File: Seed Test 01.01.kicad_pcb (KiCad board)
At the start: 2 copper layers, 124 parts, among them J1 Daisy_Seed_Temp, J10 1VOCT1_IN, J11 1VOCT2_IN, J12 MAIN_OUT1, J13 MAIN_OUT2, J14 MAIN_OUT4, J15 MAIN_OUT3, J2 DISP_3_128X64, J3 Micro_SD_Card, J4 EURO_PWR, J5 CV1_INPUT, J6 CV2_INPUT, J7 CV3_INPUT, J8 CV4_INPUT, J9 GATE_TRIGGER_IN, Q1 MMBT3904, SW1 RotaryEncoder_Switch, U1 CS4334, U2 AP2204K-3.3, U3 LM1117-5.0, U4 LM4040DBZ-5, U5 MCP6004, U6 TL074, U7 TL074, U8 MCP6002-xMC

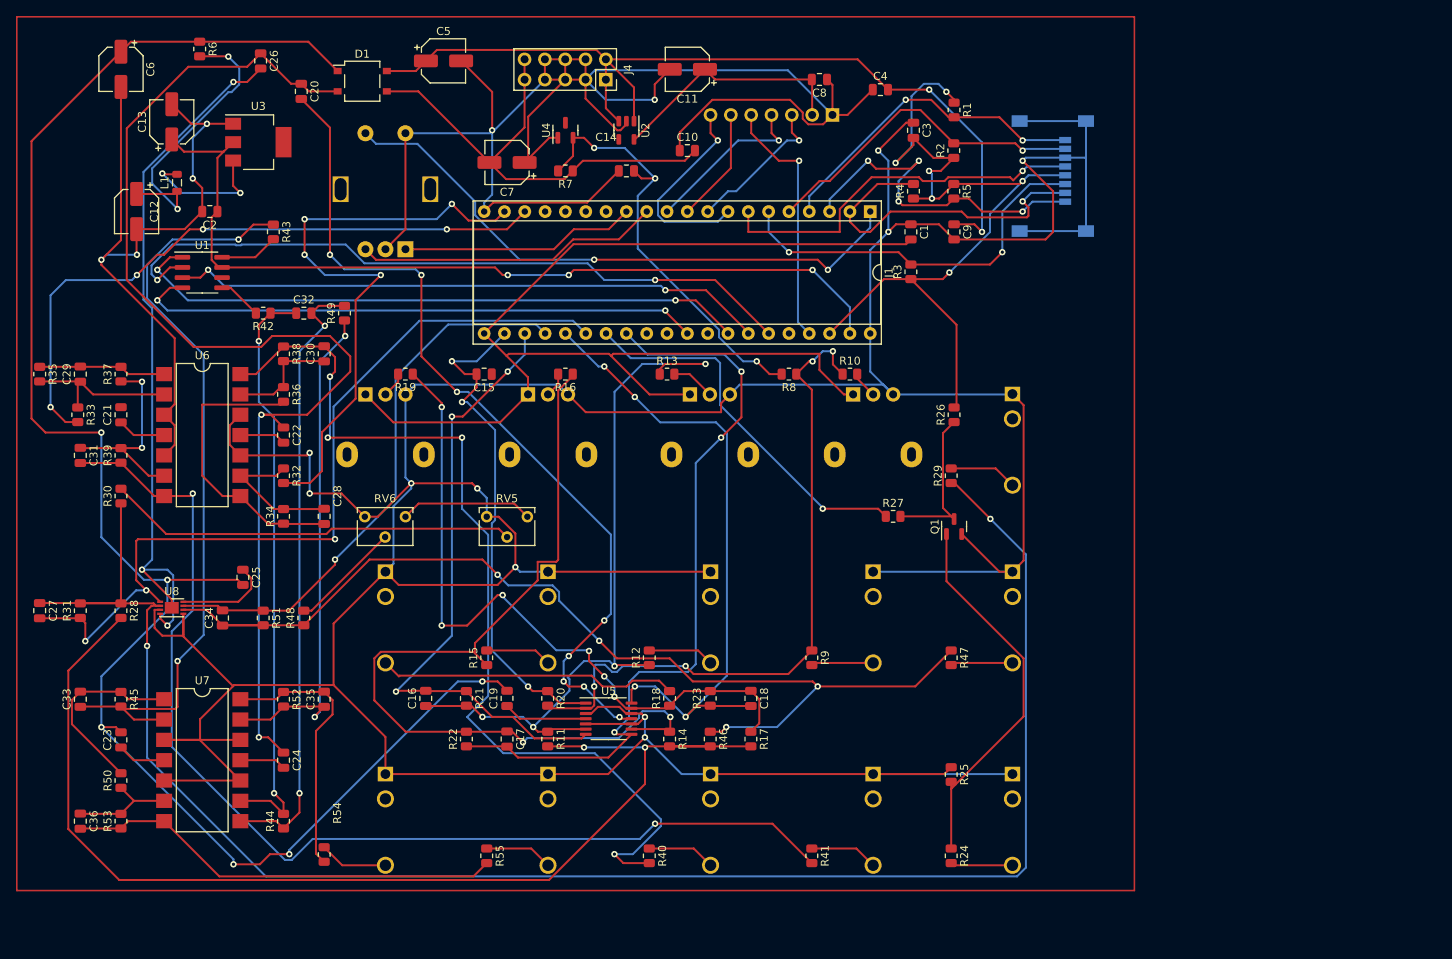
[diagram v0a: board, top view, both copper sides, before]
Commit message: updated power rails error
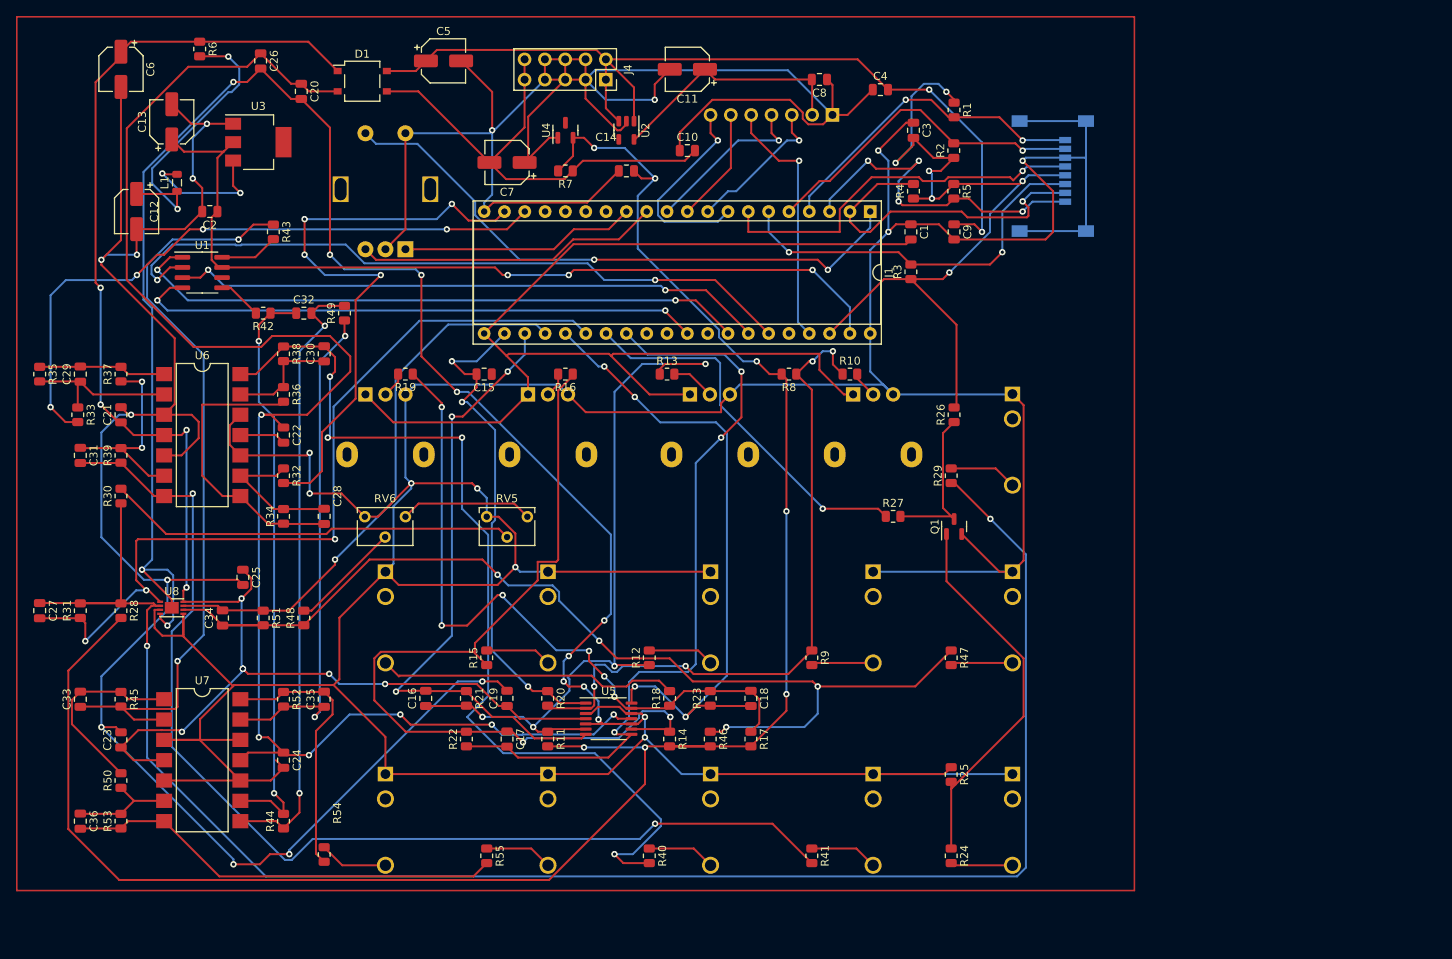
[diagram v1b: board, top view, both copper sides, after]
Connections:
- C19 pad 1: Net-(C19-Pad1) -> +12V
- C19 pad 2: +12V -> GNDA
- C20 pad 2: Net-(C20-Pad2) -> GNDA
- C21 pad 1: Net-(C21-Pad1) -> +12V
- C21 pad 2: +12V -> GNDA
- C22 pad 2: Net-(C22-Pad2) -> GNDA
- C23 pad 1: Net-(C23-Pad1) -> +12V
- C23 pad 2: +12V -> GNDA
- C24 pad 2: Net-(C24-Pad2) -> GNDA
- C25 pad 1: Net-(C25-Pad1) -> +12V
- C25 pad 2: +12V -> GNDA
- C26 pad 2: Net-(C26-Pad2) -> GNDA
- U5 pad 11: Net-(C20-Pad2) -> -12V
- U5 pad 4: Net-(C19-Pad1) -> +12V
- U6 pad 11: Net-(C22-Pad2) -> -12V
- U6 pad 4: Net-(C21-Pad1) -> +12V
- U7 pad 11: Net-(C24-Pad2) -> -12V
- U7 pad 4: Net-(C23-Pad1) -> +12V
- U8 pad 4: Net-(C26-Pad2) -> -12V
- U8 pad 8: Net-(C25-Pad1) -> +12V
- U8 pad 9: Net-(C26-Pad2) -> -12V
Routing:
- net GNDA: track 873.0 -> 1136.3 mm, vias 16 -> 30
- net -12V: track 206.5 -> 355.7 mm, vias 2 -> 9
- net Net-(C20-Pad2): track 107.7 -> 0.00 mm, vias 8 -> 0
- net Net-(C26-Pad2): track 89.6 -> 0.00 mm, vias 3 -> 0
- net -10V: track 199.0 -> 247.6 mm, vias 5 -> 7
- net +12V: track 328.2 -> 313.6 mm, vias 8 -> 12
- net Net-(C25-Pad1): track 12.0 -> 0.00 mm
- net Net-(C19-Pad1): track 10.5 -> 0.00 mm
- net Net-(C23-Pad1): track 6.05 -> 0.00 mm
- net Net-(C21-Pad1): track 6.05 -> 0.00 mm
- net Net-(C24-Pad2): track 5.79 -> 0.00 mm
- net Net-(C22-Pad2): track 5.79 -> 0.00 mm
- net Net-(C34-Pad1): track 130.1 -> 132.1 mm

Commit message: Version update
Added DC/DC power block and opAmps for audio input. Redesigned PCB completely moving all components to one side so that it can lay flat.
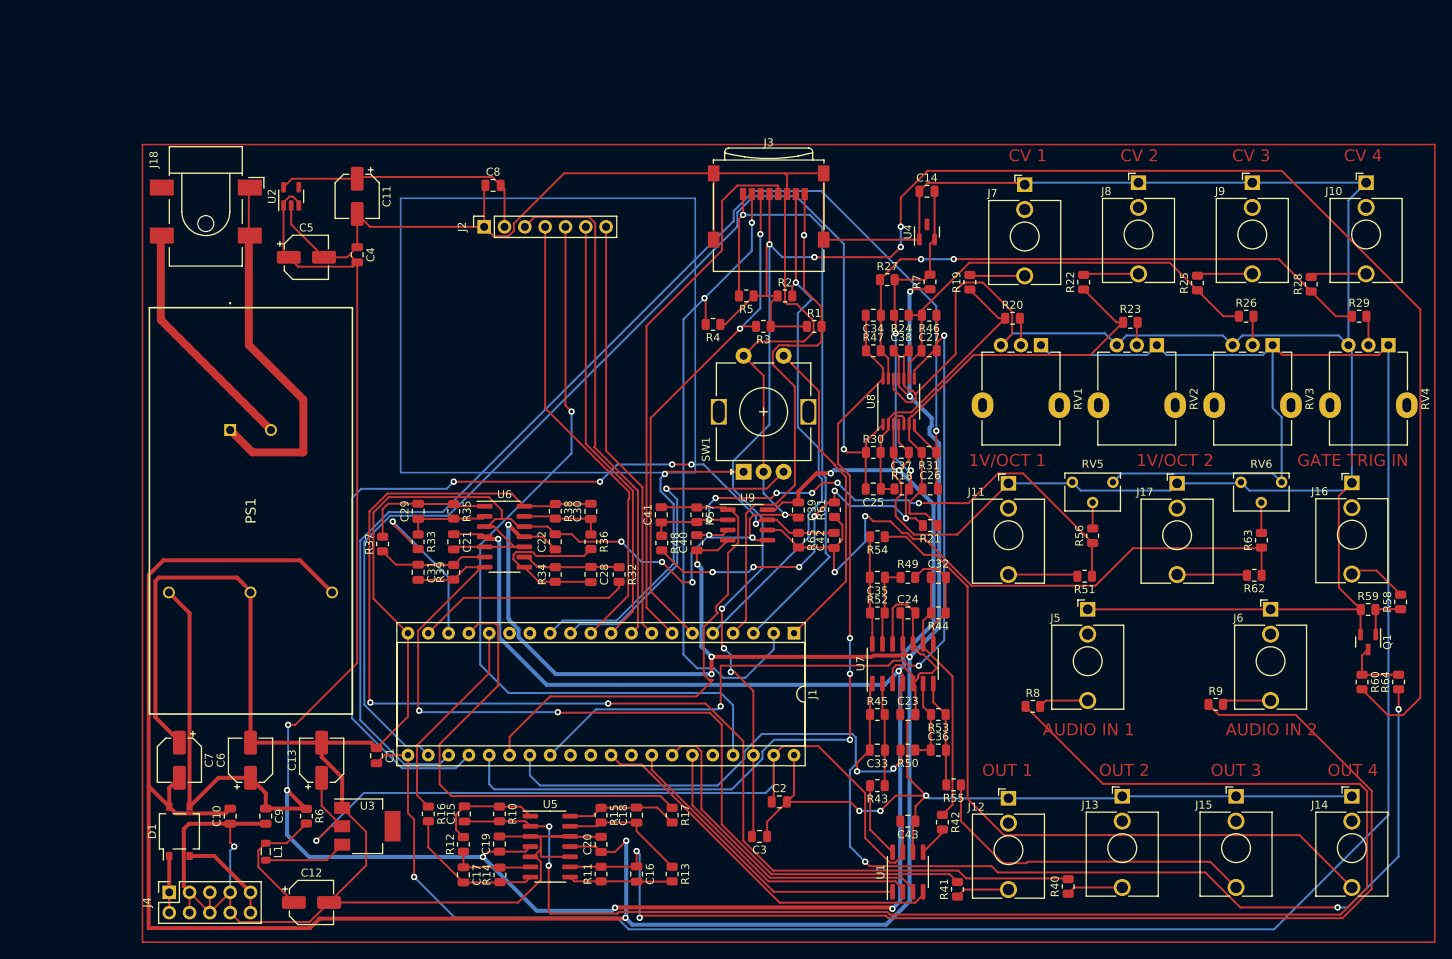
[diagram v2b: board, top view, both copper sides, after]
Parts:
- added C37: 100nF, Capacitor_SMD:C_0805_2012Metric, F.Cu at (163.9, 83.4)
- added C38: 100nF, Capacitor_SMD:C_0805_2012Metric, F.Cu at (163.9, 70.7)
- added C39: 100nF, Capacitor_SMD:C_0805_2012Metric, F.Cu at (151.0, 90.6)
- added C40: 100nF, Capacitor_SMD:C_0805_2012Metric, F.Cu at (138.3, 94.7)
- added C41: 10nF, Capacitor_SMD:C_0805_2012Metric, F.Cu at (133.9, 91.2)
- added C42: 10nF, Capacitor_SMD:C_0805_2012Metric, F.Cu at (155.5, 94.5)
- added C43: 100nF, Capacitor_SMD:C_0805_2012Metric, F.Cu at (164.7, 129.5)
- added J16: GATE_TRIGGER_IN, Connector_Audio:Jack_3.5mm_QingPu_WQP-PJ398SM_Vertical_CircularHoles, F.Cu at (220.2, 87.3)
- added J17: 1VOCT2_IN, Connector_Audio:Jack_3.5mm_QingPu_WQP-PJ398SM_Vertical_CircularHoles, F.Cu at (198.4, 87.3)
- added J18: Barrel_Jack_MountingPin, Connector_BarrelJack:BarrelJack_CLIFF_FC681465S_SMT_Horizontal, F.Cu at (77.0, 53.3)
- added PS1: DLW05A-12, KiCad:DLW05A12, F.Cu at (80.0, 80.7)
- added R56: 66.5k, Resistor_SMD:R_0805_2012Metric, F.Cu at (187.8, 93.9)
- added R57: 66.5k, Resistor_SMD:R_0805_2012Metric, F.Cu at (138.3, 91.2)
- added R58: 100k, Resistor_SMD:R_0805_2012Metric, F.Cu at (226.3, 102.1)
- added R59: 1M, Resistor_SMD:R_0805_2012Metric, F.Cu at (222.3, 103.1)
- added R60: 10k, Resistor_SMD:R_0805_2012Metric, F.Cu at (221.5, 112.1)
- added R61: 200k, Resistor_SMD:R_0805_2012Metric, F.Cu at (155.6, 90.6)
- added R62: 100k, Resistor_SMD:R_0805_2012Metric, F.Cu at (208.0, 98.8)
- added R63: 66.5k, Resistor_SMD:R_0805_2012Metric, F.Cu at (208.9, 94.4)
- added R64: 1k, Resistor_SMD:R_0805_2012Metric, F.Cu at (226.1, 112.1)
- added R65: 66.5k, Resistor_SMD:R_0805_2012Metric, F.Cu at (151.0, 94.4)
- added U9: MCP6002-xSN, Package_SO:SOIC-8_3.9x4.9mm_P1.27mm, F.Cu at (144.7, 92.5)
- C15, C16, C17, C18: value 10nF -> 47pF
- C25, C26: value 100nF -> 10nF
- J10: value 1VOCT1_IN -> CV4_INPUT; moved to F.Cu
- J11: value 1VOCT2_IN -> 1VOCT1_IN; moved to F.Cu
- J12, J13, J14, J15, J2, J3, RV1, RV2, RV3, RV4, SW1: moved to F.Cu
- J5: value CV1_INPUT -> AUDIO_IN_1L; moved to F.Cu
- J6: value CV2_INPUT -> AUDIO_IN_2R; moved to F.Cu
- J7: value CV3_INPUT -> CV1_INPUT; moved to F.Cu
- J8: value CV4_INPUT -> CV2_INPUT; moved to F.Cu
- J9: value GATE_TRIGGER_IN -> CV3_INPUT; moved to F.Cu
- R10, R13, R19, R22, R51: value 66.5k -> 100k
- R11, R14, R28, R8: value 200k -> 100k
- R16: value 66.5k -> 1k
- R17: value 200k -> 1k
- R18, R24: value 100k -> 200k
- R21, R48: value 66.5k -> 200k
- R25: value 1M -> 100k
- R26: value 10k -> 66.5k
- R27: value 1k -> 200k
- R29, R47: value 100k -> 66.5k
- R46: value 200k -> 66.5k
- U5: value MCP6004 -> TL074; footprint Package_SO:TSSOP-14_4.4x5mm_P0.65mm -> Package_SO:SOIC-14_3.9x8.7mm_P1.27mm
- U6, U7: footprint Package_DIP:SMDIP-14_W9.53mm -> Package_SO:SOIC-14_3.9x8.7mm_P1.27mm
- U8: value MCP6002-xMC -> MCP6004; footprint Package_DFN_QFN:DFN-8-1EP_3x2mm_P0.5mm_EP1.75x1.45mm -> Package_SO:TSSOP-14_4.4x5mm_P0.65mm
- moved R28 154.3 mm to (215.1, 62.4), turned to 90 degrees
- moved RV4 128.0 mm to (224.8, 70.0)
- moved J14 120.8 mm to (220.2, 126.4), turned to 0 degrees
- moved C27 115.8 mm to (167.4, 70.7), turned to 0 degrees
- moved U1 115.7 mm to (164.7, 135.9), turned to 90 degrees
- moved J4 115.3 mm to (72.4, 138.4), turned to 90 degrees
- moved C9 112.9 mm to (84.5, 128.9)
- moved RV6 109.6 mm to (211.4, 87.2)
- moved R31 107.9 mm to (167.4, 83.4), turned to 180 degrees
- moved C36 107.6 mm to (168.5, 120.7), turned to 0 degrees
- moved R42 106.1 mm to (169.0, 129.7), turned to -90 degrees
- moved J8 106.0 mm to (193.6, 49.7), turned to 0 degrees
- moved R53 103.0 mm to (168.5, 116.2), turned to 180 degrees
- moved R51 102.8 mm to (186.8, 98.9), turned to 180 degrees
- moved C2 102.5 mm to (148.7, 127.1), turned to 0 degrees
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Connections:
- C15 pad 2: ADC_CTRL_1 -> Net-(C15-Pad2)
- C16 pad 2: ADC_CTRL_2 -> Net-(C16-Pad2)
- C17 pad 2: ADC_CTRL_3 -> Net-(C17-Pad2)
- C18 pad 2: ADC_CTRL_4 -> Net-(C18-Pad2)
- C25 pad 1: +12V -> Net-(C25-Pad1)
- C25 pad 2: GNDA -> ADC_CTRL_1
- C26 pad 1: -12V -> Net-(C26-Pad1)
- C26 pad 2: GNDA -> ADC_CTRL_2
- C27 pad 2: ADC1_1VOCT1 -> ADC_CTRL_3
- C34 pad 2: ADC1_1VOCT2 -> ADC_CTRL_4
- D1 pad 1: +12V -> VCC
- D1 pad 2: -12V -> VEE
- D1 pad 3: -12V -> +12V
- D1 pad 4: +12V -> -12V
- J4 pad 1: +12V -> VCC
- J4 pad 10: -12V -> VEE
- J4 pad 2: +12V -> VCC
- J4 pad 9: -12V -> VEE
- R10 pad 1: Net-(C15-Pad1) -> Net-(C15-Pad2)
- R10 pad 2: Net-(R10-Pad2) -> Net-(C15-Pad1)
- R11 pad 1: Net-(C16-Pad1) -> Net-(C16-Pad2)
- R11 pad 2: -10V -> Net-(C16-Pad1)
- R12 pad 1: Net-(C16-Pad1) -> Net-(C17-Pad1)
- R12 pad 2: Net-(J6-PadT) -> Net-(C15-Pad2)
- R13 pad 1: Net-(C16-Pad1) -> Net-(C18-Pad1)
- R13 pad 2: Net-(R13-Pad2) -> Net-(C16-Pad2)
- R14 pad 1: Net-(C17-Pad1) -> Net-(C17-Pad2)
- R14 pad 2: -10V -> Net-(C17-Pad1)
- R15 pad 1: Net-(C17-Pad1) -> Net-(C18-Pad2)
- R15 pad 2: Net-(J7-PadT) -> Net-(C18-Pad1)
- R16 pad 1: Net-(C17-Pad1) -> AUDIO_IN_L
- R16 pad 2: Net-(R16-Pad2) -> Net-(C17-Pad2)
- R17 pad 1: Net-(C18-Pad1) -> AUDIO_IN_R
- R17 pad 2: -10V -> Net-(C18-Pad2)
- R18 pad 1: Net-(C18-Pad1) -> Net-(C25-Pad1)
- R18 pad 2: Net-(J8-PadT) -> -10V
- R19 pad 1: Net-(C18-Pad1) -> Net-(C25-Pad1)
- R19 pad 2: Net-(R19-Pad2) -> Net-(J7-PadT)
- R20 pad 1: ADC_CTRL_1 -> Net-(C25-Pad1)
- R20 pad 2: Net-(C15-Pad1) -> Net-(R20-Pad2)
- R21 pad 1: ADC_CTRL_2 -> Net-(C26-Pad1)
- R21 pad 2: Net-(C16-Pad1) -> -10V
- R22 pad 1: ADC_CTRL_3 -> Net-(C26-Pad1)
- R22 pad 2: Net-(C17-Pad1) -> Net-(J8-PadT)
- R23 pad 1: ADC_CTRL_4 -> Net-(C26-Pad1)
- R23 pad 2: Net-(C18-Pad1) -> Net-(R23-Pad2)
- R24 pad 1: Net-(Q1-Pad1) -> Net-(C27-Pad1)
- R24 pad 2: Net-(J9-PadT) -> -10V
- R25 pad 1: GNDA -> Net-(C27-Pad1)
- R25 pad 2: Net-(Q1-Pad1) -> Net-(J9-PadT)
- R26 pad 1: Net-(Q1-Pad3) -> Net-(C27-Pad1)
- R26 pad 2: +3.3VA -> Net-(R26-Pad2)
- R27 pad 1: ADC1_GATE_IN -> Net-(C34-Pad1)
- R27 pad 2: Net-(Q1-Pad3) -> -10V
- R28 pad 1: Net-(C27-Pad1) -> Net-(C34-Pad1)
- R28 pad 2: -10V -> Net-(J10-PadT)
- R29 pad 1: Net-(C27-Pad1) -> Net-(C34-Pad1)
- R29 pad 2: Net-(J10-PadT) -> Net-(R29-Pad2)
- R30 pad 1: Net-(C27-Pad1) -> ADC_CTRL_1
- R30 pad 2: Net-(R30-Pad2) -> Net-(C25-Pad1)
- R31 pad 1: ADC1_1VOCT1 -> ADC_CTRL_2
- R31 pad 2: Net-(C27-Pad1) -> Net-(C26-Pad1)
- R46 pad 1: Net-(C34-Pad1) -> ADC_CTRL_3
- R46 pad 2: -10V -> Net-(C27-Pad1)
- R47 pad 1: Net-(C34-Pad1) -> ADC_CTRL_4
- R47 pad 2: Net-(J11-PadT) -> Net-(C34-Pad1)
- R48 pad 1: Net-(C34-Pad1) -> Net-(C41-Pad1)
- R48 pad 2: Net-(R48-Pad2) -> -10V
- R51 pad 1: ADC1_1VOCT2 -> Net-(C41-Pad1)
- R51 pad 2: Net-(C34-Pad1) -> Net-(J11-PadT)
- R8 pad 2: -10V -> Net-(J5-PadT)
- R9 pad 1: Net-(C15-Pad1) -> Net-(C16-Pad1)
- R9 pad 2: Net-(J5-PadT) -> Net-(J6-PadT)
- RV1 pad 2: Net-(R10-Pad2) -> Net-(R20-Pad2)
- RV2 pad 2: Net-(R13-Pad2) -> Net-(R23-Pad2)
- RV3 pad 2: Net-(R16-Pad2) -> Net-(R26-Pad2)
- RV4 pad 2: Net-(R19-Pad2) -> Net-(R29-Pad2)
- RV5 pad 2: Net-(R30-Pad2) -> Net-(R56-Pad2)
- RV6 pad 2: Net-(R48-Pad2) -> Net-(R63-Pad2)
- U5 pad 1: ADC_CTRL_1 -> Net-(C15-Pad2)
- U5 pad 14: ADC_CTRL_4 -> Net-(C18-Pad2)
- U5 pad 6: Net-(C16-Pad1) -> Net-(C17-Pad1)
- U5 pad 7: ADC_CTRL_2 -> Net-(C17-Pad2)
- U5 pad 8: ADC_CTRL_3 -> Net-(C16-Pad2)
- U5 pad 9: Net-(C17-Pad1) -> Net-(C16-Pad1)
- U8 pad 1: ADC1_1VOCT1 -> ADC_CTRL_1
- U8 pad 2: Net-(C27-Pad1) -> Net-(C25-Pad1)
- U8 pad 4: -12V -> +12V
- U8 pad 6: Net-(C34-Pad1) -> Net-(C26-Pad1)
- U8 pad 7: ADC1_1VOCT2 -> ADC_CTRL_2
- U8 pad 8: +12V -> ADC_CTRL_3
- U8 pad 9: -12V -> Net-(C27-Pad1)
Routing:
- net GNDA: track 1136.3 -> 950.0 mm, vias 30 -> 10
- net Net-(C27-Pad1): track 221.2 -> 55.7 mm, vias 2 -> 0
- net +3.3VA: track 106.0 -> 267.1 mm, vias 6 -> 7
- net -10V: track 247.6 -> 89.8 mm, vias 7 -> 8
- net +3.3VP: track 166.7 -> 295.1 mm, vias 0 -> 1
- net ADC1_GATE_IN: track 47.6 -> 156.4 mm, vias 1 -> 3
- net Net-(C15-Pad1): track 85.1 -> 184.8 mm, vias 4 -> 2
- net Net-(C17-Pad1): track 109.8 -> 10.4 mm, vias 2 -> 0
- net ADC_CTRL_1: track 63.7 -> 149.9 mm, vias 3 -> 1
- net Net-(C42-Pad1): track 0.00 -> 84.2 mm, vias 0 -> 2
- net Net-(J14-PadT): track 8.60 -> 92.1 mm
- net Net-(C33-Pad1): track 95.9 -> 12.9 mm, vias 2 -> 0
- net ADC_CTRL_2: track 78.7 -> 160.6 mm, vias 3 -> 1
- net +12V: track 313.6 -> 394.6 mm, vias 12 -> 9
- net Net-(C18-Pad1): track 87.5 -> 15.9 mm, vias 6 -> 0
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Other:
- board text added: "1V/OCT 1"
- board text added: "1V/OCT 2"
- board text added: "AUDIO IN 1"
- board text added: "AUDIO IN 2"
- board text added: "CV 1"
- board text added: "CV 2"
- board text added: "CV 3"
- board text added: "CV 4"
- board text added: "GATE TRIG IN"
- board text added: "OUT 1"
- board text added: "OUT 2"
- board text added: "OUT 3"
- board text added: "OUT 4"

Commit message: PCB rev 1.0
PCB finished layout in 0805
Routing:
- net GNDA: track 950.0 -> 1038.1 mm, vias 10 -> 41
- added copper zone on B.Cu, net GNDA
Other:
- board outline added: 161.5 x 99.8 mm
- board text added: "v1.0"

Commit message: various updates
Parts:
- R7: value 4.7R -> 2k
- U3: value LM1117-5.0 -> LM78L05_SOT
- U4: value LM4040DBZ-5 -> LM4040DBZ-10
- moved U3 0.65 mm to (97.3, 129.5)
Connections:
- U3 pad 1: GNDA -> +5V
- U3 pad 2: +5V -> GNDA
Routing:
- net GNDA: track 1038.1 -> 1040.5 mm, vias 41 -> 84
- net ADC1_1VOCT1: track 63.8 -> 61.9 mm
- net +5V: track 111.5 -> 113.2 mm
- net OLED_RST: track 99.7 -> 100.7 mm
- added copper zone on F.Cu, net GNDA
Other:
- board text added: "v1.01"
- board text removed: "v1.0"
